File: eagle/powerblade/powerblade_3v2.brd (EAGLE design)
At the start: 25.4 x 25.4 mm, 79 parts, among them J1 JTAG_14PIN_IDC-ND, J2 AC_INF3, J4 TC2030-JLINK-NL, Q1 NTS4173, Q4 2SK1829, U1 TPS62122, U2 MCP6V3, U3 MSP430FR5738, U4 NRF51822QF, U6 MAX9910, U7 OPA2369, X1 16MHz, X3 32.768kHz, Y1 UREACH_XTEND

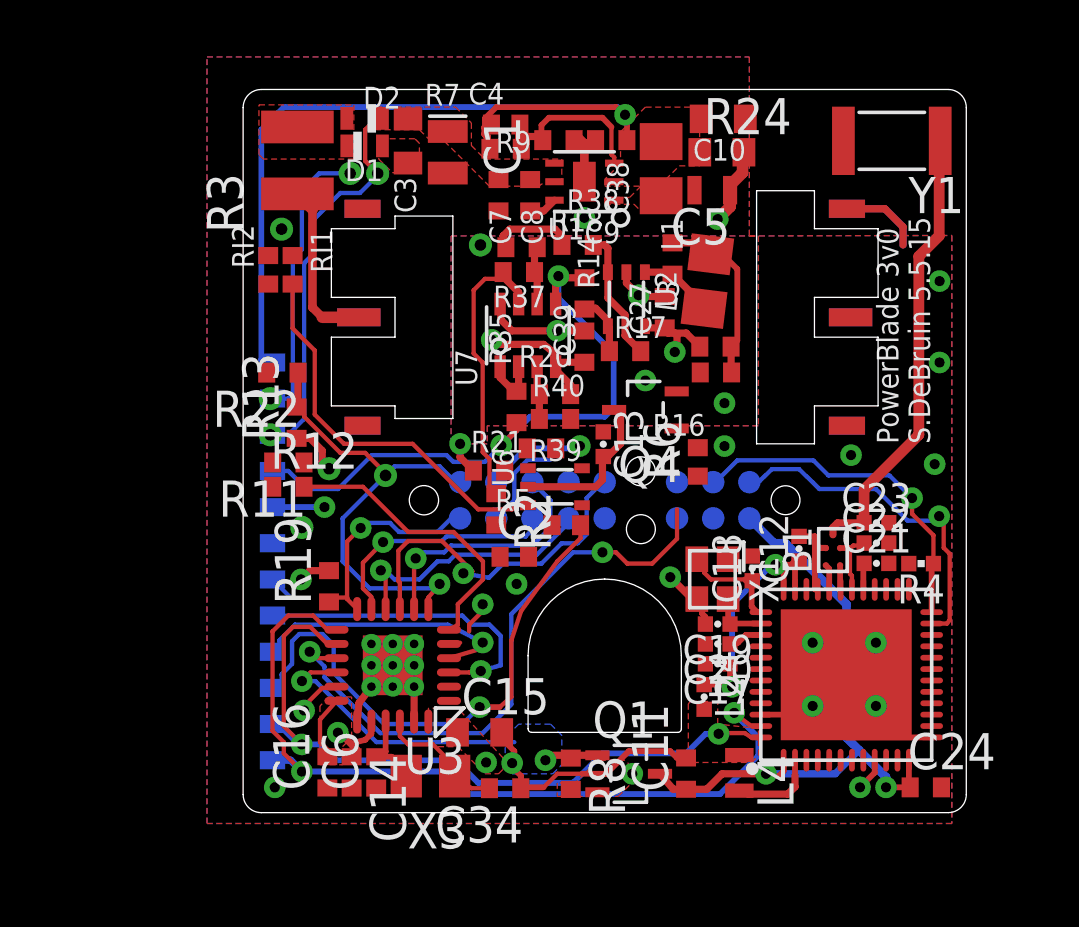
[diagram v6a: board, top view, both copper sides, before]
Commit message: more routing in powerblade
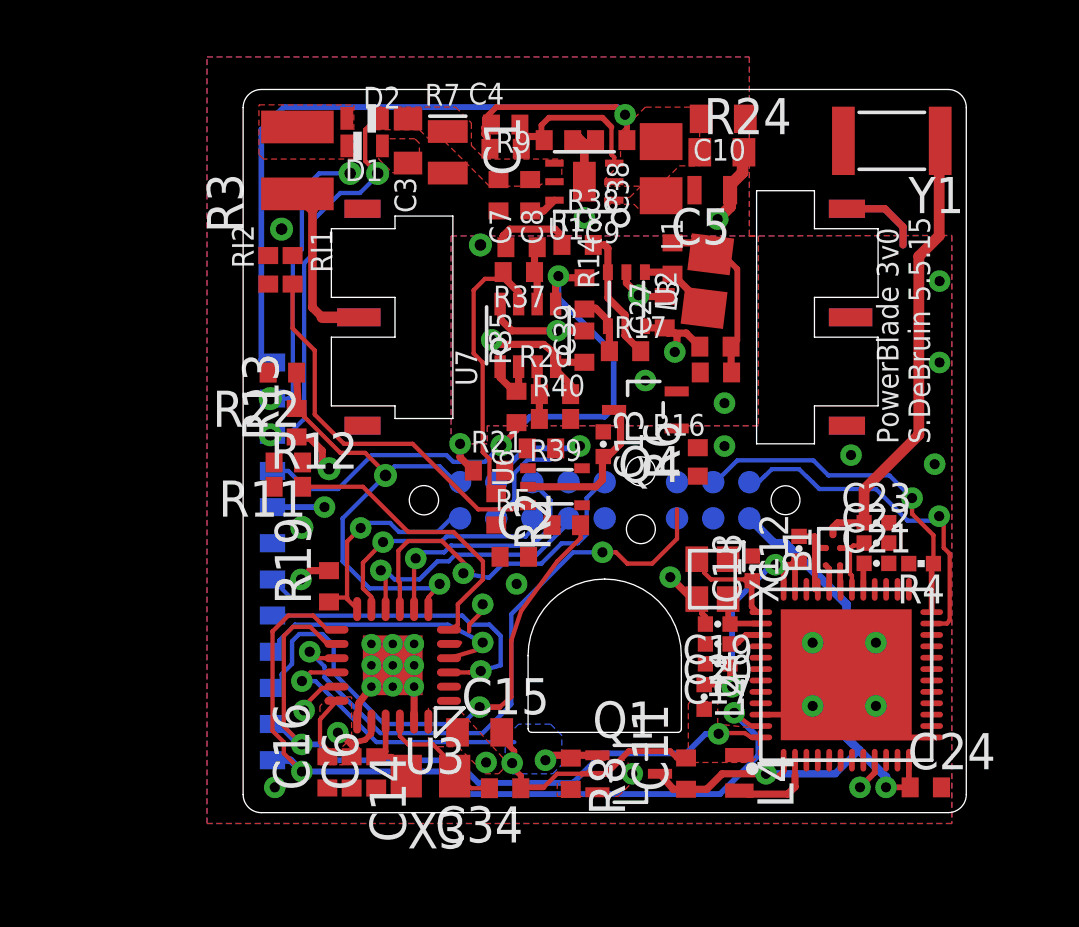
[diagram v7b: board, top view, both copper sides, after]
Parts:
- R11, R12, R13, R22, R9: device rcl:R0402_SM -> rcl:R0402
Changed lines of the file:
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@@
 <attribute name="DIGIKEY" value="P560KLCT-ND" x="-3.4798" y="6.7691" size="1.778" layer="27" rot="R180" display="off"/>
 </element>
-<element name="R9" library="rcl" package="R0402_SM" value="180k" x="-1.6256" y="6.223" smashed="yes" rot="R180">
+<element name="R9" library="rcl" package="R0402" value="180k" x="-1.6256" y="6.223" smashed="yes" rot="R180">
 <attribute name="NAME" x="-2.5781" y="6.5405" size="0.762" layer="25" rot="R180"/>
 <attribute name="DIGIKEY" value="P180KLCT-ND" x="-1.6256" y="6.223" size="1.778" layer="27" rot="R180" display="off"/>
@@
 <attribute name="DIGIKEY" value="NP" x="-2.54" y="21.7678" size="1.778" layer="28" rot="MR180" display="off"/>
 </element>
-<element name="R11" library="rcl" package="R0402_SM" value="670k" x="-11.1125" y="-5.09905" rot="R180">
+<element name="R11" library="rcl" package="R0402" value="670k" x="-11.1125" y="-5.09905" rot="R180">
 <attribute name="DIGIKEY" value="P665KLCT-ND" x="-11.1125" y="-5.09905" size="1.778" layer="27" rot="R180" display="off"/>
 </element>
-<element name="R12" library="rcl" package="R0402_SM" value="330k" x="-11.1125" y="-5.953125">
+<element name="R12" library="rcl" package="R0402" value="330k" x="-11.1125" y="-5.953125">
 <attribute name="DIGIKEY" value="P330KLCT-ND" x="-11.1125" y="-5.953125" size="1.778" layer="27" display="off"/>
 </element>
@@
 <attribute name="DIGIKEY" value="P665KLCT-ND" x="3.27025" y="-5.08" size="1.778" layer="27" rot="R90" display="off"/>
 </element>
-<element name="R13" library="rcl" package="R0402_SM" value="330k" x="-10.8204" y="-3.70205" rot="R90">
+<element name="R13" library="rcl" package="R0402" value="330k" x="-10.8204" y="-3.70205" rot="R90">
 <attribute name="DIGIKEY" value="P330KLCT-ND" x="-10.8204" y="-3.70205" size="1.778" layer="27" rot="R90" display="off"/>
 </element>
-<element name="R22" library="rcl" package="R0402_SM" value="670k" x="-11.32205" y="-1.9431" rot="R180">
+<element name="R22" library="rcl" package="R0402" value="670k" x="-11.32205" y="-1.9431" rot="R180">
 <attribute name="DIGIKEY" value="P665KLCT-ND" x="-11.32205" y="-1.9431" size="1.778" layer="27" rot="R180" display="off"/>
 </element>
@@
 <wire x1="-8.594725" y1="4.365625" x2="-7.9756" y2="4.98475" width="0.1524" layer="16"/>
 <wire x1="-7.9756" y1="4.98475" x2="-7.9756" y2="5.051425" width="0.1524" layer="16"/>
-<wire x1="-11.668125" y1="-4.1275" x2="-11.6625" y2="-5.09905" width="0" layer="19" extent="1-16"/>
+<wire x1="-11.668125" y1="-4.1275" x2="-11.6125" y2="-5.09905" width="0" layer="19" extent="1-16"/>
 </signal>
 <signal name="ZC">
@@
 <wire x1="-10.95375" y1="-2.69875" x2="-10.95375" y2="2.06375" width="0.1524" layer="16"/>
 <wire x1="-10.95375" y1="2.06375" x2="-10.63625" y2="2.38125" width="0.1524" layer="16"/>
-<wire x1="-11.668125" y1="-2.8575" x2="-11.87205" y2="-1.9431" width="0" layer="19" extent="1-16"/>
+<wire x1="-11.668125" y1="-2.8575" x2="-11.82205" y2="-1.9431" width="0" layer="19" extent="1-16"/>
 <wire x1="-9.0578" y1="6.0198" x2="-8.9408" y2="5.051425" width="0" layer="19" extent="1-1"/>
 </signal>
@@
 <wire x1="-3.021875" y1="6.35" x2="-2.9298" y2="5.9182" width="0.254" layer="1"/>
 <wire x1="-2.2225" y1="6.35" x2="-3.021875" y2="6.35" width="0.254" layer="1"/>
-<wire x1="-2.2225" y1="6.35" x2="-2.1756" y2="6.223" width="0.254" layer="1"/>
+<wire x1="-2.2225" y1="6.35" x2="-2.1256" y2="6.223" width="0.254" layer="1"/>
 <wire x1="-1.958975" y1="7.0104" x2="-0.079375" y2="7.0104" width="0.2032" layer="1"/>
 </signal>
@@
 <wire x1="-5.3086" y1="-7.540625" x2="-6.905625" y2="-7.540625" width="0.1524" layer="1"/>
 <wire x1="-6.905625" y1="-7.540625" x2="-8.493125" y2="-5.953125" width="0.1524" layer="1"/>
-<wire x1="-8.493125" y1="-5.953125" x2="-10.5625" y2="-5.953125" width="0.1524" layer="1"/>
-<wire x1="-10.5625" y1="-5.953125" x2="-10.5625" y2="-5.09905" width="0" layer="19" extent="1-1"/>
+<wire x1="-8.493125" y1="-5.953125" x2="-10.6125" y2="-5.953125" width="0.1524" layer="1"/>
+<wire x1="-10.6125" y1="-5.953125" x2="-10.6125" y2="-5.09905" width="0" layer="19" extent="1-1"/>
 </signal>
 <signal name="N$3">
@@
 <contactref element="R22" pad="1"/>
 <contactref element="R13" pad="2"/>
-<wire x1="-10.8204" y1="-3.15205" x2="-10.77205" y2="-3.1037" width="0.254" layer="1"/>
-<wire x1="-10.77205" y1="-3.1037" x2="-10.77205" y2="-1.9431" width="0.254" layer="1"/>
+<wire x1="-10.8204" y1="-3.20205" x2="-10.77205" y2="-3.1037" width="0.254" layer="1"/>
+<wire x1="-10.77205" y1="-3.1037" x2="-10.82205" y2="-1.9431" width="0.254" layer="1"/>
 <via x="-7.699375" y="-5.55625" extent="1-16" drill="0.4064"/>
-<wire x1="-10.8204" y1="-3.15205" x2="-10.556875" y2="-3.415575" width="0.1524" layer="1"/>
+<wire x1="-10.8204" y1="-3.20205" x2="-10.556875" y2="-3.415575" width="0.1524" layer="1"/>
 <wire x1="-10.556875" y1="-3.415575" x2="-10.556875" y2="-3.4925" width="0.1524" layer="1"/>
 <wire x1="-10.556875" y1="-3.4925" x2="-9.286875" y2="-4.7625" width="0.1524" layer="1"/>
@@
 <wire x1="-0.714375" y1="4.7625" x2="-0.714375" y2="6.111875" width="0.3048" layer="1"/>
 <wire x1="-0.714375" y1="6.111875" x2="-0.9525" y2="6.35" width="0.3048" layer="1"/>
-<wire x1="-0.9525" y1="6.35" x2="-1.0756" y2="6.223" width="0.3048" layer="1"/>
+<wire x1="-0.9525" y1="6.35" x2="-1.1256" y2="6.223" width="0.3048" layer="1"/>
 <via x="8.651875" y="-4.841875" extent="1-16" drill="0.3556"/>
 <via x="4.206875" y="-4.524375" extent="1-16" drill="0.3556"/>
@@
 <via x="-10.63625" y="-7.381875" extent="1-16" drill="0.4064"/>
 <via x="-9.68375" y="-5.318125" extent="1-16" drill="0.4064"/>
-<wire x1="-10.8204" y1="-4.25205" x2="-10.35295" y2="-4.25205" width="0.254" layer="1"/>
+<wire x1="-10.8204" y1="-4.20205" x2="-10.35295" y2="-4.25205" width="0.254" layer="1"/>
 <wire x1="-10.35295" y1="-4.25205" x2="-9.921875" y2="-4.683125" width="0.254" layer="1"/>
 <wire x1="-9.921875" y1="-4.683125" x2="-9.921875" y2="-5.08" width="0.254" layer="1"/>

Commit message: updated most 0402 to new footprint
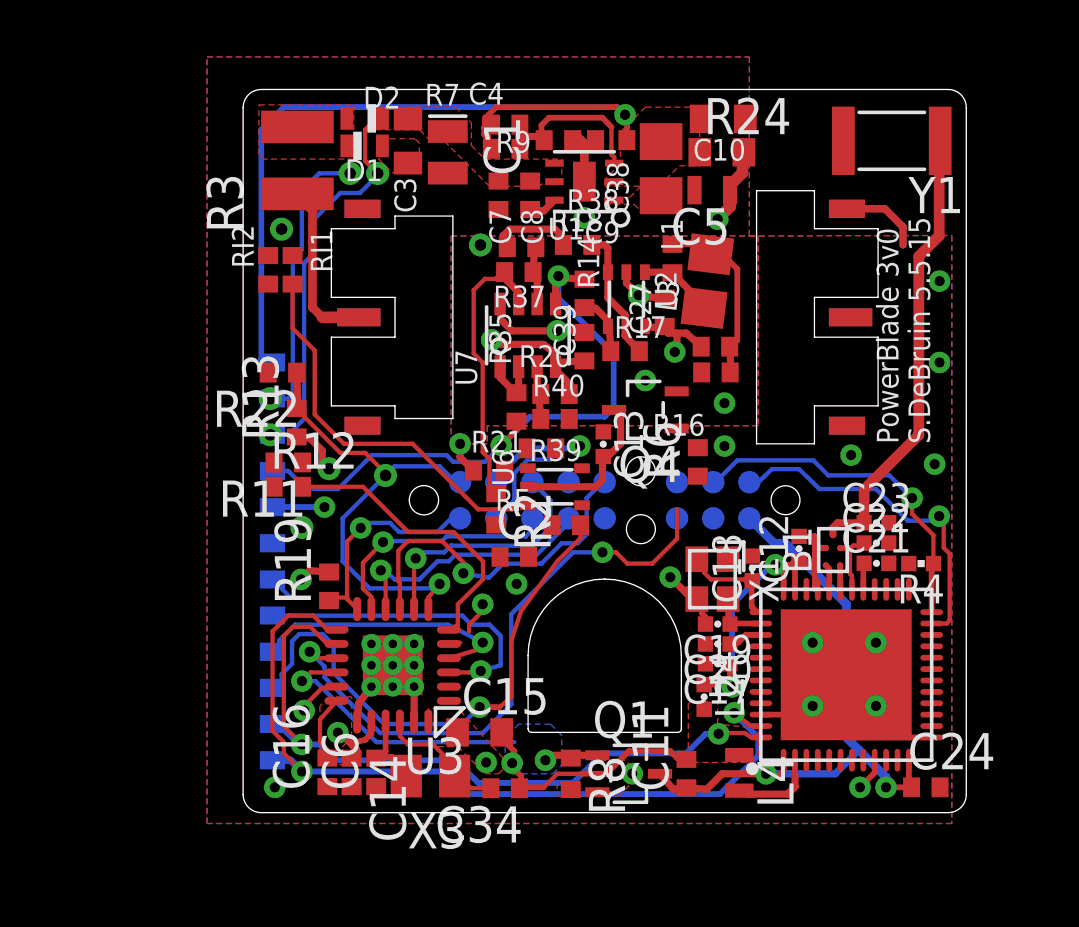
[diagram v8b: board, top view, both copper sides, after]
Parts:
- C11, C14, C16, C24, C27, C34, C38, C39, C4, C6, C7, C8: device rcl:C0402_SM -> rcl:C0402
- C5: value 22uF -> NP
- R14, R15, R16, R17, R18, R19, R35, R37, R38, R39, R40: device rcl:R0402_SM -> rcl:R0402
